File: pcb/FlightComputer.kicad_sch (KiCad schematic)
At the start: 74 parts, among them J1 USB4105-GF-A, Q1 DMG3415U, Q2 Si2302CDS, Q3 Si2302CDS, SW1 RESET, SW2 BOOT, U2 ICM-42670-P, U3 ESP32-C3-MINI-1, U5 SY8088, U6 MCP73831T-2ACI/OT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

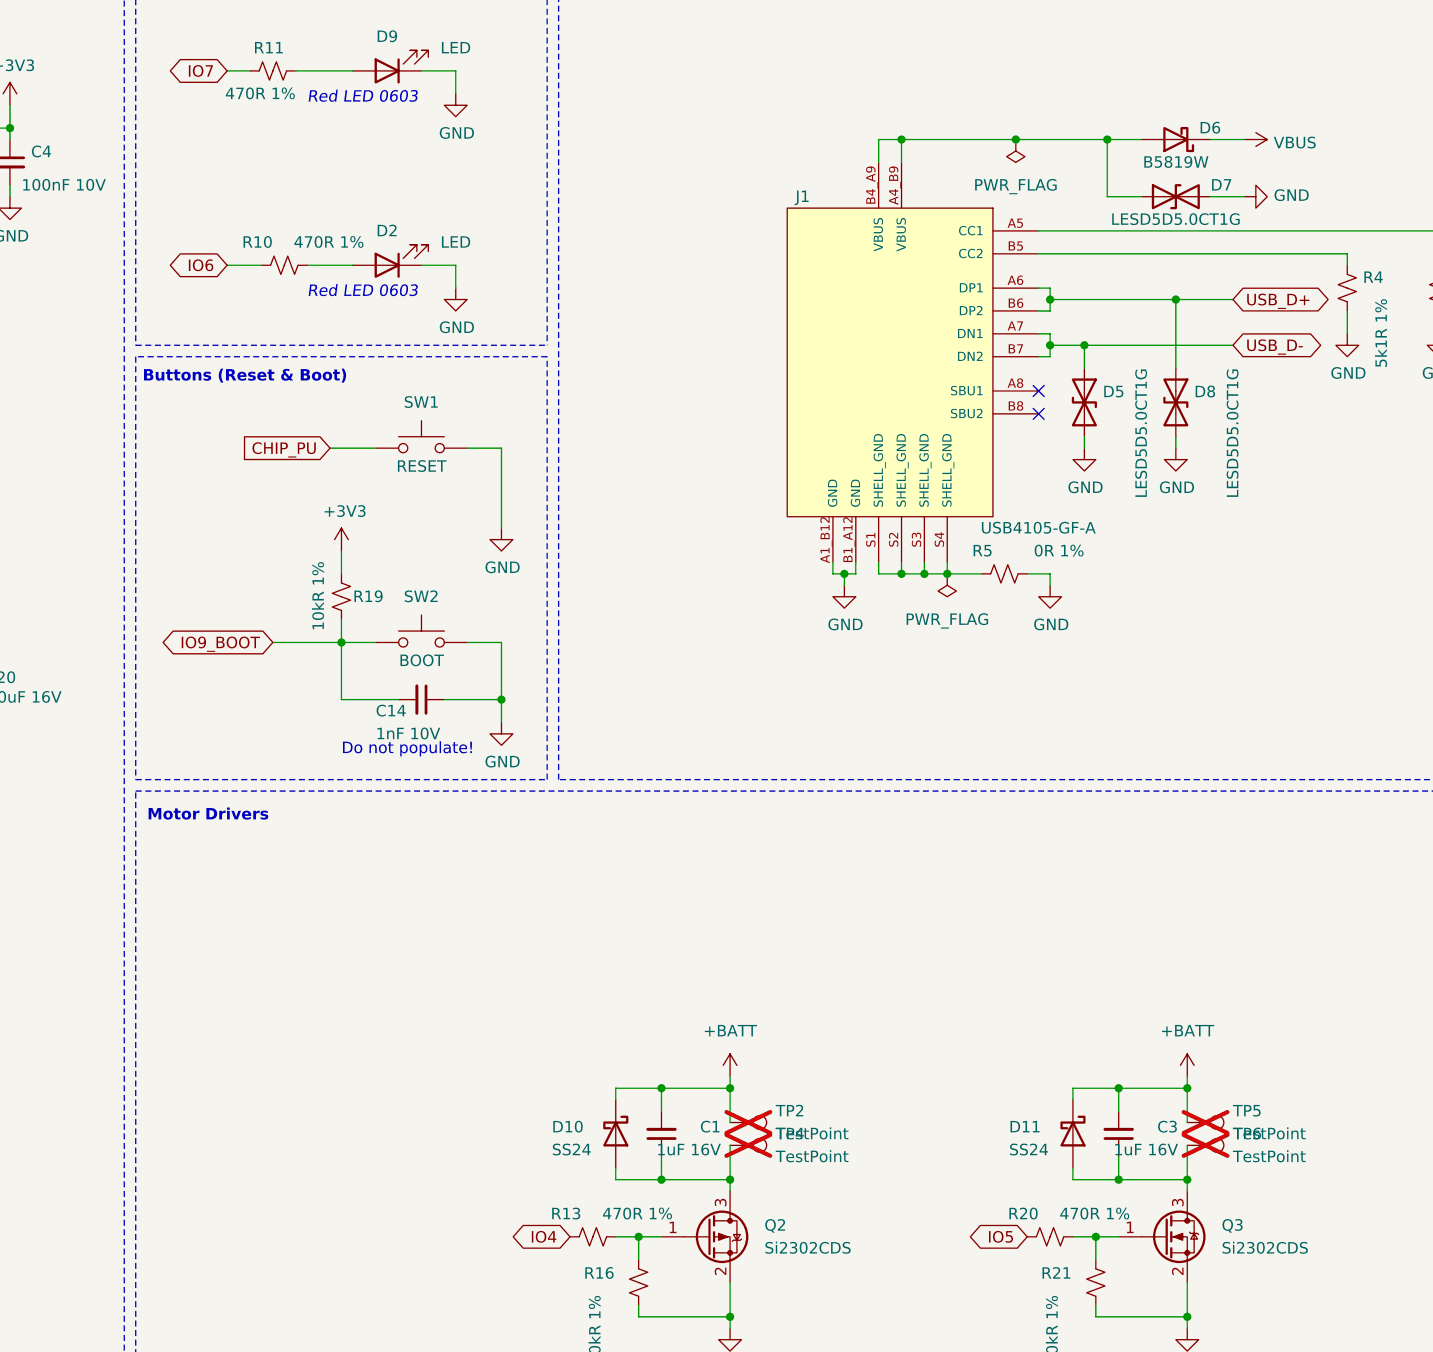
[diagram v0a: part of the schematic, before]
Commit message: Add GND vias, clean up schematic
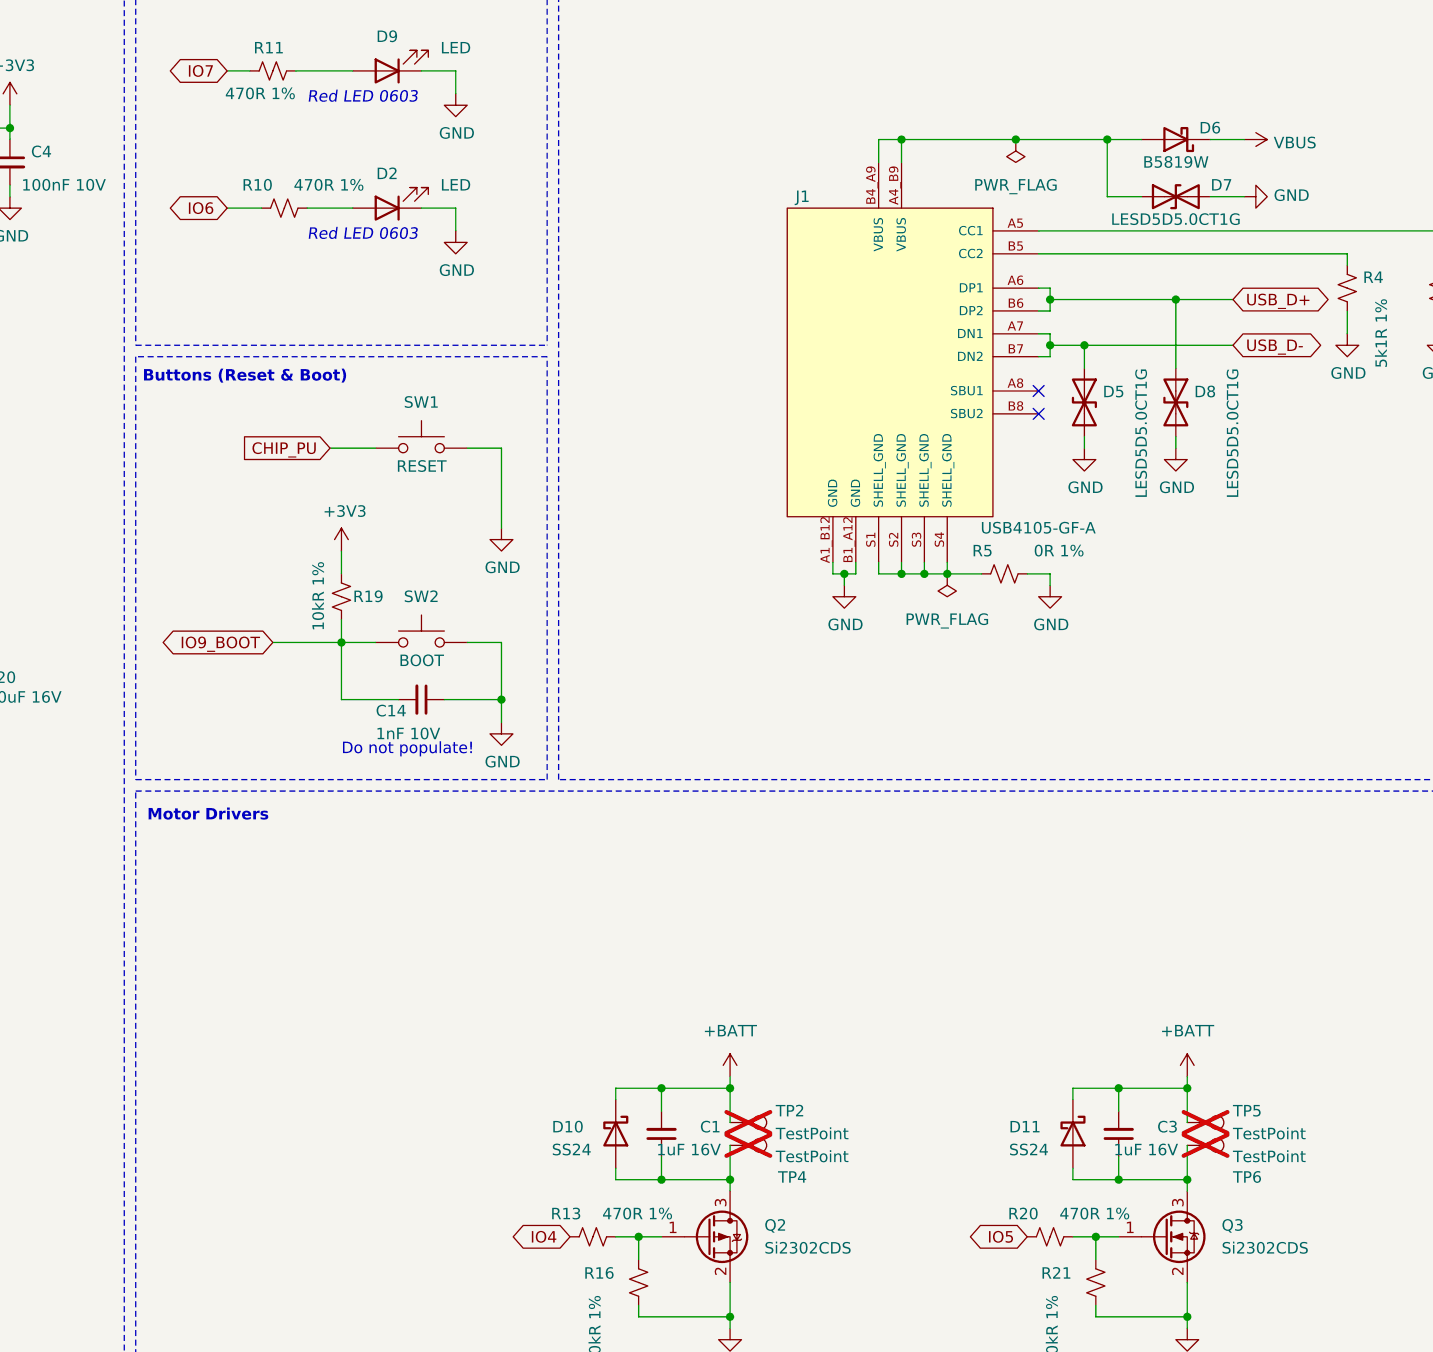
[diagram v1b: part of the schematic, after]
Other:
- moved on the sheet: D2, R10
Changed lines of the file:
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@@
 	(wire
 		(pts
-			(xy 146.05 139.7) (xy 149.86 139.7)
+			(xy 146.05 133.35) (xy 149.86 133.35)
 		)
 		(stroke
@@
 	(wire
 		(pts
-			(xy 124.46 139.7) (xy 128.27 139.7)
+			(xy 124.46 133.35) (xy 128.27 133.35)
 		)
 		(stroke
@@
 	(wire
 		(pts
-			(xy 133.35 139.7) (xy 138.43 139.7)
+			(xy 133.35 133.35) (xy 138.43 133.35)
 		)
 		(stroke
@@
 	(wire
 		(pts
-			(xy 149.86 139.7) (xy 149.86 142.24)
+			(xy 149.86 133.35) (xy 149.86 135.89)
 		)
 		(stroke
@@
 	(text "Red LED 0603"
 		(exclude_from_sim no)
-		(at 133.35 143.51 0)
+		(at 133.35 137.16 0)
 		(effects
 			(font
@@
 	(global_label "IO6"
 		(shape bidirectional)
-		(at 124.46 139.7 180)
+		(at 124.46 133.35 180)
 		(fields_autoplaced yes)
 		(effects
@@
 		)
 		(property "Intersheetrefs" "${INTERSHEET_REFS}"
-			(at 118.0317 139.7 0)
+			(at 118.0317 133.35 0)
 			(effects
 				(font
@@
 	(symbol
 		(lib_id "Device:LED")
-		(at 142.24 139.7 180)
+		(at 142.24 133.35 180)
 		(unit 1)
 		(exclude_from_sim no)
@@
 		(dnp no)
 		(property "Reference" "D2"
-			(at 142.24 135.89 0)
+			(at 142.24 129.54 0)
 			(effects
 				(font
@@
 		)
 		(property "Value" "LED"
-			(at 149.86 137.16 0)
+			(at 149.86 130.81 0)
 			(effects
 				(font
@@
 		)
 		(property "Footprint" "LED_SMD:LED_0603_1608Metric"
-			(at 142.24 139.7 0)
+			(at 142.24 133.35 0)
 			(effects
 				(font
@@
 		)
 		(property "Datasheet" "~"
-			(at 142.24 139.7 0)
+			(at 142.24 133.35 0)
 			(effects
 				(font
@@
 		)
 		(property "Description" ""
-			(at 142.24 139.7 0)
+			(at 142.24 133.35 0)
 			(effects
 				(font
@@
 		)
 		(property "LCSC" "C2286"
-			(at 142.24 139.7 0)
+			(at 142.24 133.35 0)
 			(effects
 				(font
@@
 	(symbol
 		(lib_id "Device:R_Small_US")
-		(at 130.81 139.7 90)
+		(at 130.81 133.35 90)
 		(unit 1)
 		(exclude_from_sim no)
@@
 		(dnp no)
 		(property "Reference" "R10"
-			(at 129.54 137.16 90)
+			(at 129.54 130.81 90)
 			(effects
 				(font
@@
 		)
 		(property "Value" "470R 1%"
-			(at 139.7 137.16 90)
+			(at 139.7 130.81 90)
 			(effects
 				(font
@@
 		)
 		(property "Footprint" "Resistor_SMD:R_0402_1005Metric"
-			(at 130.81 139.7 0)
+			(at 130.81 133.35 0)
 			(effects
 				(font
@@
 		)
 		(property "Datasheet" "~"
-			(at 130.81 139.7 0)
+			(at 130.81 133.35 0)
 			(effects
 				(font
@@
 		)
 		(property "Description" ""
-			(at 130.81 139.7 0)
+			(at 130.81 133.35 0)
 			(effects
 				(font
@@
 		)
 		(property "LCSC" "C25117"
-			(at 130.81 139.7 0)
+			(at 130.81 133.35 0)
 			(effects
 				(font
@@
 	(symbol
 		(lib_id "power:GND")
-		(at 149.86 142.24 0)
+		(at 149.86 135.89 0)
 		(unit 1)
 		(exclude_from_sim no)
@@
 		(dnp no)
 		(property "Reference" "#PWR0136"
-			(at 149.86 148.59 0)
+			(at 149.86 142.24 0)
 			(effects
 				(font
@@
 		)
 		(property "Value" "GND"
-			(at 149.987 146.6342 0)
+			(at 149.987 140.2842 0)
 			(effects
 				(font
@@
 		)
 		(property "Footprint" ""
-			(at 149.86 142.24 0)
+			(at 149.86 135.89 0)
 			(effects
 				(font
@@
 		)
 		(property "Datasheet" ""
-			(at 149.86 142.24 0)
+			(at 149.86 135.89 0)
 			(effects
 				(font
@@
 		)
 		(property "Description" "Power symbol creates a global label with name \"GND\" , ground"
-			(at 149.86 142.24 0)
+			(at 149.86 135.89 0)
 			(effects
 				(font
@@
 		(on_board yes)
 		(dnp yes)
-		(fields_autoplaced yes)
 		(property "Reference" "TP6"
-			(at 236.22 236.2199 90)
+			(at 236.22 241.046 90)
 			(effects
 				(font
@@
 		(on_board yes)
 		(dnp yes)
-		(fields_autoplaced yes)
 		(property "Reference" "TP4"
-			(at 185.42 236.2199 90)
+			(at 185.674 241.046 90)
 			(effects
 				(font

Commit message: Update FlightComputer.kicad_sch
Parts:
- removed TP2, TP4, TP5, TP6: TestPoint, TestPoint:TestPoint_Pad_D2.0mm, symbol Connector:TestPoint
- added J2: Conn_01x02_Pin, Connector_JST:JST_SHL_SM02B-SHLS-TF_1x02-1MP_P1.00mm_Horizontal, symbol Connector:Conn_01x02_Pin
- added J3: Conn_01x02_Pin, Connector_JST:JST_PH_B2B-PH-K_1x02_P2.00mm_Vertical, symbol Connector:Conn_01x02_Pin
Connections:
- net +BATT: now also J2.2 (Pin_2), J3.2 (Pin_2)
- net at C1.1, D10.2 (A), Q2.3 (D): now also J2.1 (Pin_1)
- net at C3.1, D11.2 (A), Q3.3 (D): now also J3.1 (Pin_1)
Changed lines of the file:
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@@
+	)
+	(symbol
+		(lib_id "Connector:Conn_01x02_Pin")
+		(at 236.22 237.49 180)
+		(unit 1)
+		(exclude_from_sim no)
+		(in_bom yes)
+		(on_board yes)
+		(dnp no)
+		(fields_autoplaced yes)
+		(property "Reference" "J3"
+			(at 237.49 234.9499 0)
+			(effects
+				(font
+					(size 1.27 1.27)
+				)
+				(justify right)
+			)
+		)
+		(property "Value" "Conn_01x02_Pin"
+			(at 237.49 237.4899 0)
+			(effects
+				(font
+					(size 1.27 1.27)
+				)
+				(justify right)
+			)
+		)
+		(property "Footprint" "Connector_JST:JST_PH_B2B-PH-K_1x02_P2.00mm_Vertical"
+			(at 236.22 237.49 0)
+			(effects
+				(font
+					(size 1.27 1.27)
+				)
+				(hide yes)
+			)
+		)
+		(property "Datasheet" "~"
+			(at 236.22 237.49 0)
+			(effects
+				(font
+					(size 1.27 1.27)
+				)
+				(hide yes)
+			)
+		)
+		(property "Description" "Generic connector, single row, 01x02, script generated"
+			(at 236.22 237.49 0)
+			(effects
+				(font
+					(size 1.27 1.27)
+				)
+				(hide yes)
+			)
+		)
+		(pin "1"
+		)
+		(pin "2"
+		)
+		(instances
+			(project "FlightComputer"
+				(path "/196a8dd5-5fd6-4c7f-ae4a-0104bd82e61b"
+					(reference "J3")
+					(unit 1)
+				)
+			)
+		)
 	)
 	(symbol
@@
 				(path "/196a8dd5-5fd6-4c7f-ae4a-0104bd82e61b"
 					(reference "D10")
-					(unit 1)
-				)
-			)
-		)
-	)
-	(symbol
-		(lib_id "Connector:TestPoint")
-		(at 180.34 234.95 270)
-		(unit 1)
-		(exclude_from_sim no)
-		(in_bom yes)
-		(on_board yes)
-		(dnp yes)
-		(fields_autoplaced yes)
-		(property "Reference" "TP2"
-			(at 185.42 233.6799 90)
-			(effects
-				(font
-					(size 1.27 1.27)
-				)
-				(justify left)
-			)
-		)
-		(property "Value" "TestPoint"
-			(at 185.42 236.2199 90)
-			(effects
-				(font
-					(size 1.27 1.27)
-				)
-				(justify left)
-			)
-		)
-		(property "Footprint" "TestPoint:TestPoint_Pad_D2.0mm"
-			(at 180.34 240.03 0)
-			(effects
-				(font
-					(size 1.27 1.27)
-				)
-				(hide yes)
-			)
-		)
-		(property "Datasheet" "~"
-			(at 180.34 240.03 0)
-			(effects
-				(font
-					(size 1.27 1.27)
-				)
-				(hide yes)
-			)
-		)
-		(property "Description" "test point"
-			(at 180.34 234.95 0)
-			(effects
-				(font
-					(size 1.27 1.27)
-				)
-				(hide yes)
-			)
-		)
-		(pin "1"
-		)
-		(instances
-			(project "FlightComputer"
-				(path "/196a8dd5-5fd6-4c7f-ae4a-0104bd82e61b"
-					(reference "TP2")
 					(unit 1)
 				)
@@
 				(path "/196a8dd5-5fd6-4c7f-ae4a-0104bd82e61b"
 					(reference "SW1")
+					(unit 1)
+				)
+			)
+		)
+	)
+	(symbol
+		(lib_id "Connector:Conn_01x02_Pin")
+		(at 185.42 237.49 180)
+		(unit 1)
+		(exclude_from_sim no)
+		(in_bom yes)
+		(on_board yes)
+		(dnp no)
+		(fields_autoplaced yes)
+		(property "Reference" "J2"
+			(at 186.69 234.9499 0)
+			(effects
+				(font
+					(size 1.27 1.27)
+				)
+				(justify right)
+			)
+		)
+		(property "Value" "Conn_01x02_Pin"
+			(at 186.69 237.4899 0)
+			(effects
+				(font
+					(size 1.27 1.27)
+				)
+				(justify right)
+			)
+		)
+		(property "Footprint" "Connector_JST:JST_SHL_SM02B-SHLS-TF_1x02-1MP_P1.00mm_Horizontal"
+			(at 185.42 237.49 0)
+			(effects
+				(font
+					(size 1.27 1.27)
+				)
+				(hide yes)
+			)
+		)
+		(property "Datasheet" "~"
+			(at 185.42 237.49 0)
+			(effects
+				(font
+					(size 1.27 1.27)
+				)
+				(hide yes)
+			)
+		)
+		(property "Description" "Generic connector, single row, 01x02, script generated"
+			(at 185.42 237.49 0)
+			(effects
+				(font
+					(size 1.27 1.27)
+				)
+				(hide yes)
+			)
+		)
+		(pin "1"
+		)
+		(pin "2"
+		)
+		(instances
+			(project ""
+				(path "/196a8dd5-5fd6-4c7f-ae4a-0104bd82e61b"
+					(reference "J2")
 					(unit 1)
 				)
@@
 	)
 	(symbol
-		(lib_id "Connector:TestPoint")
-		(at 231.14 234.95 270)
-		(unit 1)
-		(exclude_from_sim no)
-		(in_bom yes)
-		(on_board yes)
-		(dnp yes)
-		(fields_autoplaced yes)
-		(property "Reference" "TP5"
-			(at 236.22 233.6799 90)
-			(effects
-				(font
-					(size 1.27 1.27)
-				)
-				(justify left)
-			)
-		)
-		(property "Value" "TestPoint"
-			(at 236.22 236.2199 90)
-			(effects
-				(font
-					(size 1.27 1.27)
-				)
-				(justify left)
-			)
-		)
-		(property "Footprint" "TestPoint:TestPoint_Pad_D2.0mm"
-			(at 231.14 240.03 0)
-			(effects
-				(font
-					(size 1.27 1.27)
-				)
-				(hide yes)
-			)
-		)
-		(property "Datasheet" "~"
-			(at 231.14 240.03 0)
-			(effects
-				(font
-					(size 1.27 1.27)
-				)
-				(hide yes)
-			)
-		)
-		(property "Description" "test point"
-			(at 231.14 234.95 0)
-			(effects
-				(font
-					(size 1.27 1.27)
-				)
-				(hide yes)
-			)
-		)
-		(pin "1"
-		)
-		(instances
-			(project "FlightComputer"
-				(path "/196a8dd5-5fd6-4c7f-ae4a-0104bd82e61b"
-					(reference "TP5")
-					(unit 1)
-				)
-			)
-		)
-	)
-	(symbol
 		(lib_id "power:GND")
 		(at 95.25 190.5 0)
@@
 	)
 	(symbol
-		(lib_id "Connector:TestPoint")
-		(at 231.14 237.49 270)
-		(unit 1)
-		(exclude_from_sim no)
-		(in_bom yes)
-		(on_board yes)
-		(dnp yes)
-		(property "Reference" "TP6"
-			(at 236.22 241.046 90)
-			(effects
-				(font
-					(size 1.27 1.27)
-				)
-				(justify left)
-			)
-		)
-		(property "Value" "TestPoint"
-			(at 236.22 238.7599 90)
-			(effects
-				(font
-					(size 1.27 1.27)
-				)
-				(justify left)
-			)
-		)
-		(property "Footprint" "TestPoint:TestPoint_Pad_D2.0mm"
-			(at 231.14 242.57 0)
-			(effects
-				(font
-					(size 1.27 1.27)
-				)
-				(hide yes)
-			)
-		)
-		(property "Datasheet" "~"
-			(at 231.14 242.57 0)
-			(effects
-				(font
-					(size 1.27 1.27)
-				)
-				(hide yes)
-			)
-		)
-		(property "Description" "test point"
-			(at 231.14 237.49 0)
-			(effects
-				(font
-					(size 1.27 1.27)
-				)
-				(hide yes)
-			)
-		)
-		(pin "1"
-		)
-		(instances
-			(project "FlightComputer"
-				(path "/196a8dd5-5fd6-4c7f-ae4a-0104bd82e61b"
-					(reference "TP6")
-					(unit 1)
-				)
-			)
-		)
-	)
-	(symbol
 		(lib_id "Device:C_Small")
 		(at 68.58 186.69 0)
@@
 					(unit 1)
 				)
-			)
-		)
-	)
-	(symbol
-		(lib_id "Connector:TestPoint")
-		(at 180.34 237.49 270)
-		(unit 1)
-		(exclude_from_sim no)
-		(in_bom yes)
-		(on_board yes)
-		(dnp yes)
-		(property "Reference" "TP4"
-			(at 185.674 241.046 90)
-			(effects
-				(font
-					(size 1.27 1.27)
-				)
-				(justify left)
-			)
-		)
-		(property "Value" "TestPoint"
-			(at 185.42 238.7599 90)
-			(effects
-				(font
-					(size 1.27 1.27)
-				)
-				(justify left)
-			)
-		)
-		(property "Footprint" "TestPoint:TestPoint_Pad_D2.0mm"
-			(at 180.34 242.57 0)
-			(effects
-				(font
-					(size 1.27 1.27)
-				)
-				(hide yes)
-			)
-		)
-		(property "Datasheet" "~"
-			(at 180.34 242.57 0)
-			(effects
-				(font
-					(size 1.27 1.27)
-				)
-				(hide yes)
-			)
-		)
-		(property "Description" "test point"
-			(at 180.34 237.49 0)
-			(effects
-				(font
-					(size 1.27 1.27)
-				)
-				(hide yes)
-			)
-		)
-		(pin "1"
-		)
-		(instances
-			(project "FlightComputer"
-				(path "/196a8dd5-5fd6-4c7f-ae4a-0104bd82e61b"
-					(reference "TP4")
-					(unit 1)
-				)
